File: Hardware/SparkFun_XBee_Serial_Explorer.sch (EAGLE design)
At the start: 45 parts, among them Q1 MBT2222, U1 MAX232SOIC16, U2 XBEE-1B3, U3 LM317

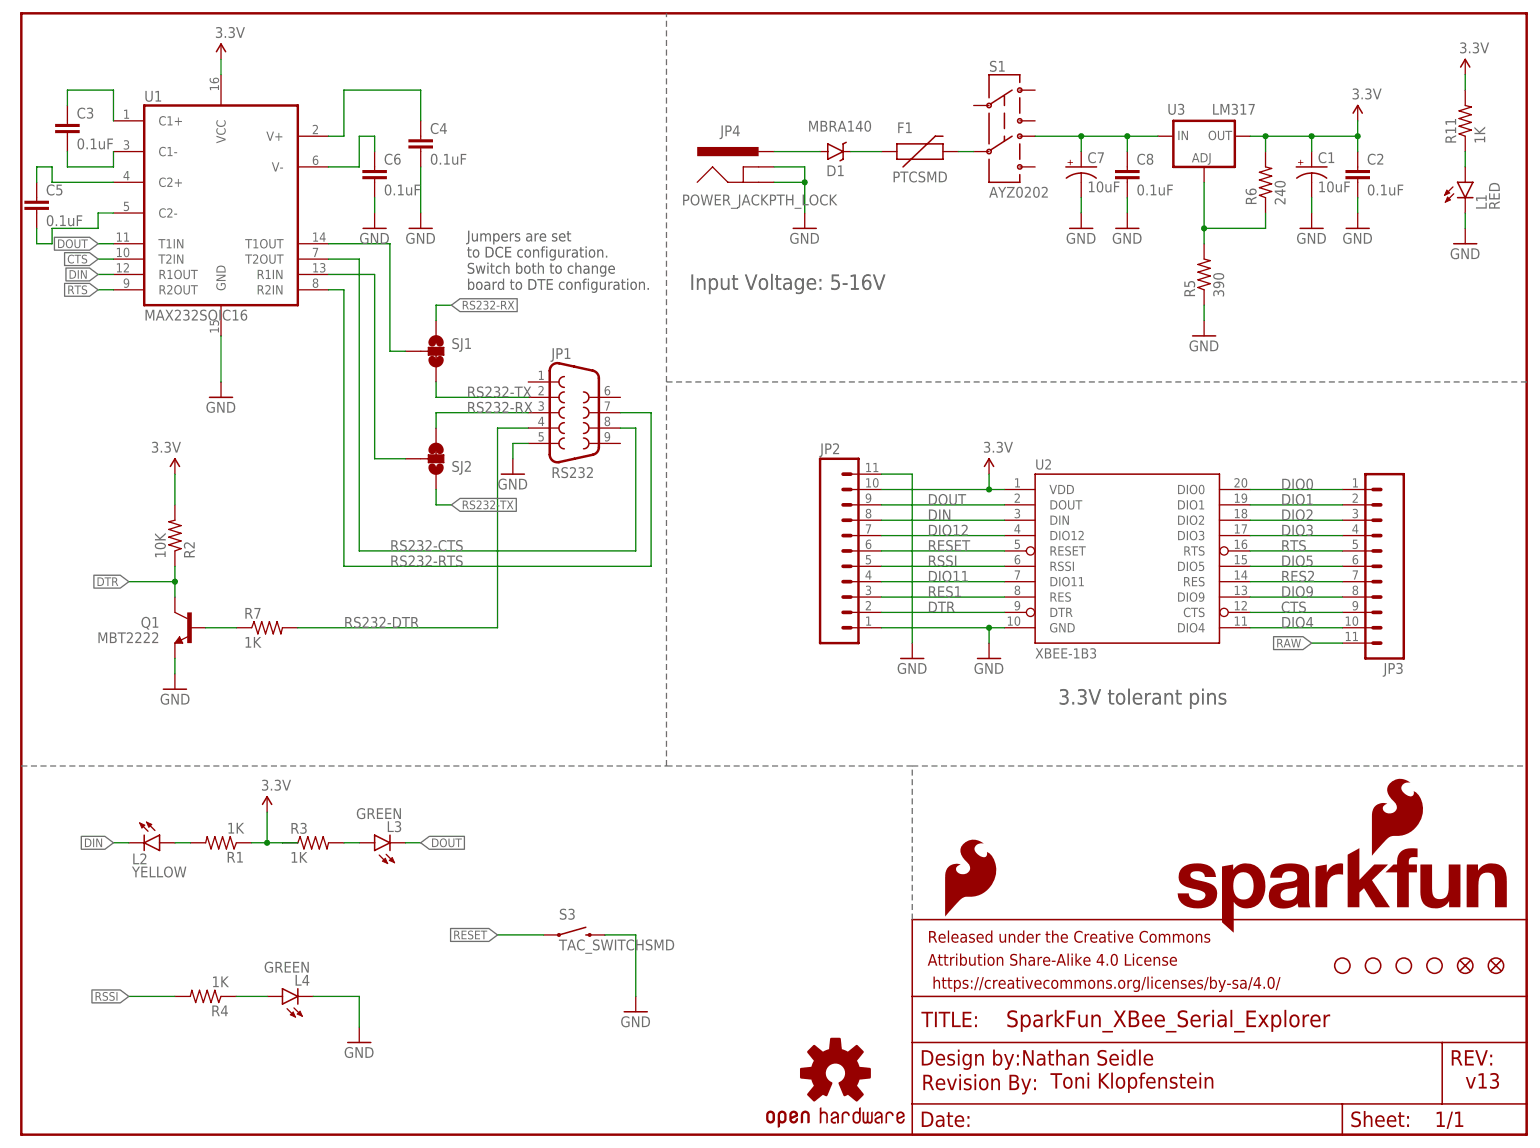
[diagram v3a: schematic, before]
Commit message: Fixes for QC checklist
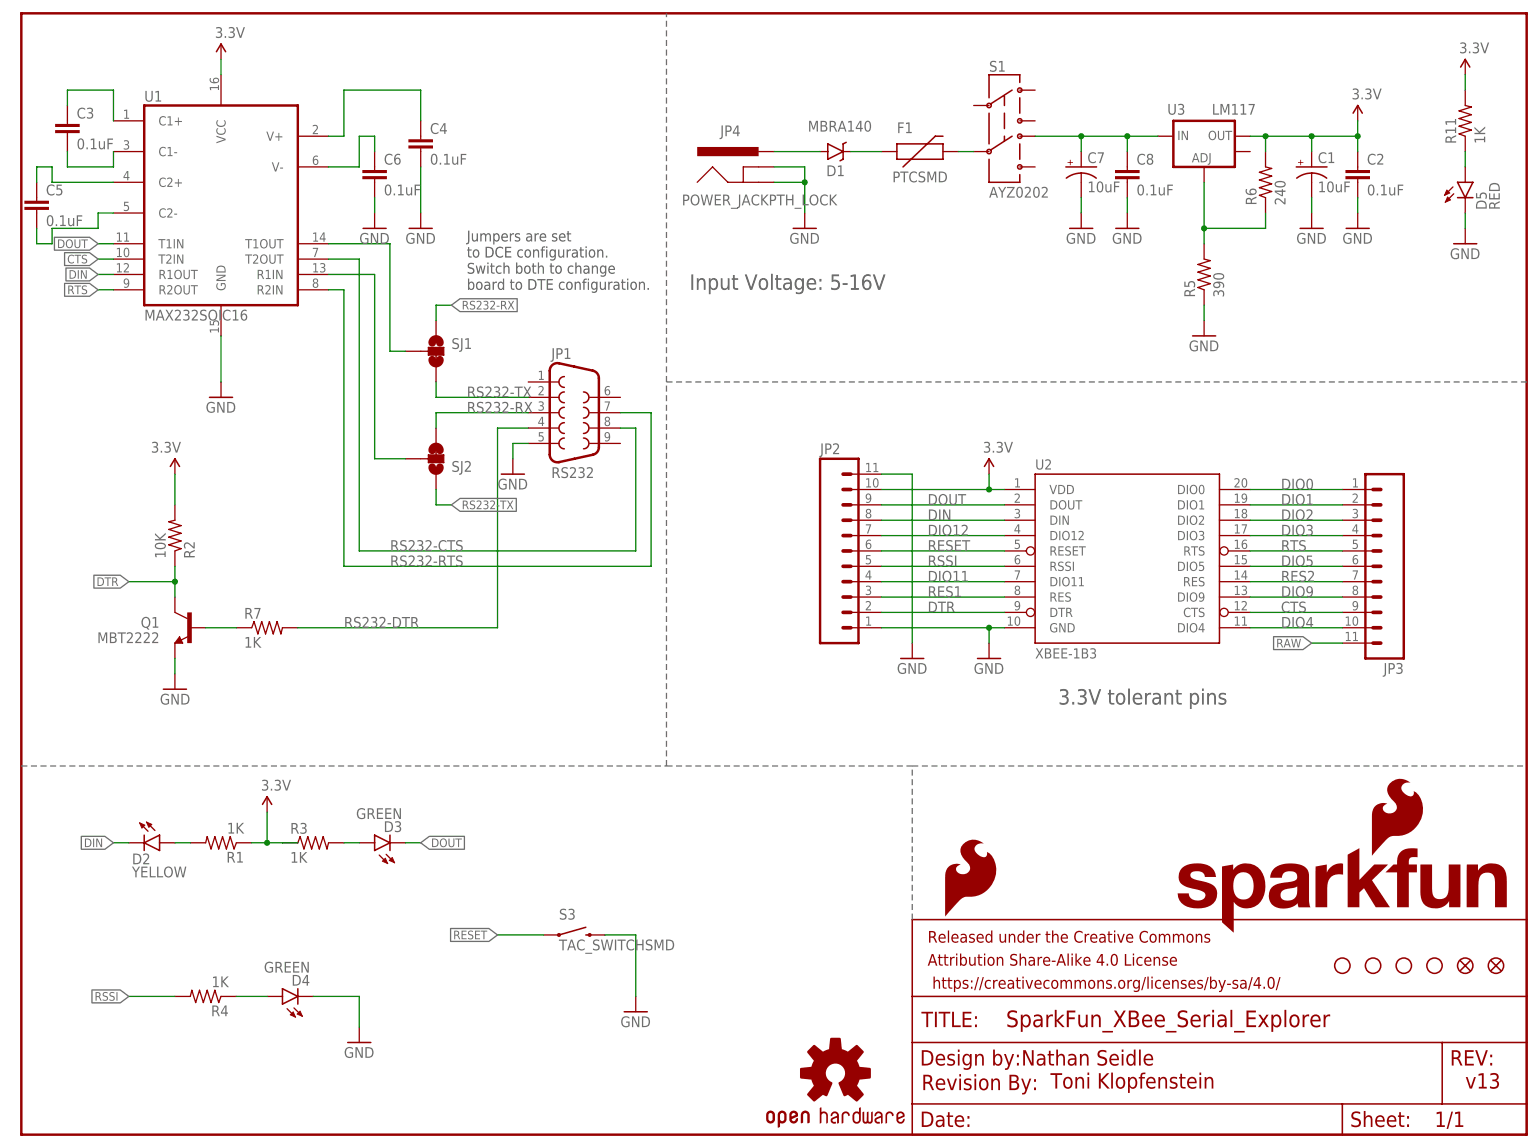
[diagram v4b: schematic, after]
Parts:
- U3: value LM317 -> LM117; device SparkFun:V_REG_317SMD -> SparkFun-PowerIC:V_REG_LM1117SOT223
- renumbered L1 to D5, L2 to D2, L3 to D3, L4 to D4
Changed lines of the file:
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@@
 <setting verticaltext="up"/>
 </settings>
-<grid distance="0.05" unitdist="inch" unit="inch" style="lines" multiple="1" display="no" altdistance="0.005" altunitdist="inch" altunit="inch"/>
+<grid distance="0.1" unitdist="inch" unit="inch" style="lines" multiple="1" display="no" altdistance="0.01" altunitdist="inch" altunit="inch"/>
 <layers>
 <layer number="1" name="Top" color="4" fill="1" visible="no" active="no"/>
@@
 </attributes>
 <variantdefs>
+<variantdef name="Attributes"/>
 </variantdefs>
 <classes>
@@
 <part name="FRAME1" library="SparkFun-Aesthetics" deviceset="FRAME-LETTER" device=""/>
 <part name="R11" library="SparkFun-Resistors" deviceset="1KOHM-1/10W-1%(0603)" device="" value="1K"/>
-<part name="L1" library="SparkFun-LED" deviceset="LED-RED" device="1206" value="RED"/>
+<part name="D5" library="SparkFun-LED" deviceset="LED-RED" device="1206" value="RED"/>
 <part name="GND28" library="SparkFun-Aesthetics" deviceset="GND" device=""/>
-<part name="L2" library="SparkFun-LED" deviceset="LED-YELLOW" device="LARGE" value="YELLOW"/>
-<part name="L3" library="SparkFun-LED" deviceset="LED-GREEN" device="LARGE" value="GREEN"/>
+<part name="D2" library="SparkFun-LED" deviceset="LED-YELLOW" device="LARGE" value="YELLOW"/>
+<part name="D3" library="SparkFun-LED" deviceset="LED-GREEN" device="LARGE" value="GREEN"/>
 <part name="R1" library="SparkFun-Resistors" deviceset="1KOHM-1/10W-1%(0603)" device="" value="1K"/>
 <part name="R3" library="SparkFun-Resistors" deviceset="1KOHM-1/10W-1%(0603)" device="" value="1K"/>
@@
 <part name="U$10" library="SparkFun-Electromechanical" deviceset="STAND-OFF" device=""/>
 <part name="U$11" library="SparkFun-Electromechanical" deviceset="STAND-OFF" device=""/>
-<part name="L4" library="SparkFun-LED" deviceset="LED-GREEN" device="LARGE" value="GREEN"/>
+<part name="D4" library="SparkFun-LED" deviceset="LED-GREEN" device="LARGE" value="GREEN"/>
 <part name="R4" library="SparkFun-Resistors" deviceset="1KOHM-1/10W-1%(0603)" device="" value="1K"/>
 <part name="GND4" library="SparkFun-Aesthetics" deviceset="GND" device=""/>
@@
 <part name="P+6" library="SparkFun" deviceset="3.3V" device=""/>
 <part name="GND13" library="SparkFun-Aesthetics" deviceset="GND" device=""/>
-<part name="U3" library="SparkFun" deviceset="V_REG_317" device="SMD" value="LM317"/>
+<part name="U3" library="SparkFun-PowerIC" deviceset="V_REG_LM1117" device="SOT223" value="LM117"/>
 <part name="R5" library="SparkFun-Resistors" deviceset="390OHM1/10W1%(0603)" device="" value="390"/>
 <part name="R6" library="SparkFun-Resistors" deviceset="240OHM1/10W1%(0603)" device="" value="240"/>
@@
 <instance part="FRAME1" gate="G$2" x="147.32" y="0"/>
 <instance part="R11" gate="G$1" x="238.76" y="167.64" rot="R90"/>
-<instance part="L1" gate="G$1" x="238.76" y="157.48"/>
+<instance part="D5" gate="G$1" x="238.76" y="157.48"/>
 <instance part="GND28" gate="1" x="238.76" y="147.32"/>
-<instance part="L2" gate="G$1" x="22.86" y="48.26" rot="R270"/>
-<instance part="L3" gate="G$1" x="58.42" y="48.26" rot="R90"/>
+<instance part="D2" gate="G$1" x="22.86" y="48.26" rot="R270"/>
+<instance part="D3" gate="G$1" x="58.42" y="48.26" rot="R90"/>
 <instance part="R1" gate="G$1" x="33.02" y="48.26" rot="R180"/>
 <instance part="R3" gate="G$1" x="48.26" y="48.26"/>
@@
 <instance part="U$10" gate="G$1" x="223.52" y="27.94"/>
 <instance part="U$11" gate="G$1" x="218.44" y="27.94"/>
-<instance part="L4" gate="G$1" x="43.18" y="22.86" rot="R90"/>
+<instance part="D4" gate="G$1" x="43.18" y="22.86" rot="R90"/>
 <instance part="R4" gate="G$1" x="30.48" y="22.86" rot="R180"/>
 <instance part="GND4" gate="1" x="55.88" y="15.24"/>
@@
 <segment>
 <wire x1="238.76" y1="152.4" x2="238.76" y2="149.86" width="0.1524" layer="91"/>
-<pinref part="L1" gate="G$1" pin="C"/>
+<pinref part="D5" gate="G$1" pin="C"/>
 <pinref part="GND28" gate="1" pin="GND"/>
 </segment>
@@
 <wire x1="48.26" y1="22.86" x2="55.88" y2="22.86" width="0.1524" layer="91"/>
 <wire x1="55.88" y1="22.86" x2="55.88" y2="17.78" width="0.1524" layer="91"/>
-<pinref part="L4" gate="G$1" pin="C"/>
+<pinref part="D4" gate="G$1" pin="C"/>
 <pinref part="GND4" gate="1" pin="GND"/>
 </segment>
@@
 <wire x1="238.76" y1="160.02" x2="238.76" y2="162.56" width="0.1524" layer="91"/>
 <pinref part="R11" gate="G$1" pin="1"/>
-<pinref part="L1" gate="G$1" pin="A"/>
+<pinref part="D5" gate="G$1" pin="A"/>
 </segment>
 </net>
@@
 <segment>
 <wire x1="27.94" y1="48.26" x2="25.4" y2="48.26" width="0.1524" layer="91"/>
-<pinref part="L2" gate="G$1" pin="A"/>
+<pinref part="D2" gate="G$1" pin="A"/>
 <pinref part="R1" gate="G$1" pin="2"/>
 </segment>
@@
 <segment>
 <wire x1="53.34" y1="48.26" x2="55.88" y2="48.26" width="0.1524" layer="91"/>
-<pinref part="L3" gate="G$1" pin="A"/>
+<pinref part="D3" gate="G$1" pin="A"/>
 <pinref part="R3" gate="G$1" pin="2"/>
 </segment>
@@
 <segment>
 <wire x1="17.78" y1="48.26" x2="15.24" y2="48.26" width="0.1524" layer="91"/>
-<pinref part="L2" gate="G$1" pin="C"/>
+<pinref part="D2" gate="G$1" pin="C"/>
 <label x="15.24" y="48.26" size="1.4224" layer="95" rot="R180" xref="yes"/>
 </segment>
@@
 <segment>
 <wire x1="63.5" y1="48.26" x2="66.04" y2="48.26" width="0.1524" layer="91"/>
-<pinref part="L3" gate="G$1" pin="C"/>
+<pinref part="D3" gate="G$1" pin="C"/>
 <label x="66.04" y="48.26" size="1.4224" layer="95" xref="yes"/>
 </segment>
@@
 <segment>
 <wire x1="35.56" y1="22.86" x2="40.64" y2="22.86" width="0.1524" layer="91"/>
-<pinref part="L4" gate="G$1" pin="A"/>
+<pinref part="D4" gate="G$1" pin="A"/>
 <pinref part="R4" gate="G$1" pin="1"/>
 </segment>
